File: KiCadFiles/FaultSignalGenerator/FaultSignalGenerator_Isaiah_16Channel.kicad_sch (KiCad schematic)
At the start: 18 parts, among them J1 Conn_02x20_Odd_Even, J2 Conn_02x16_Odd_Even

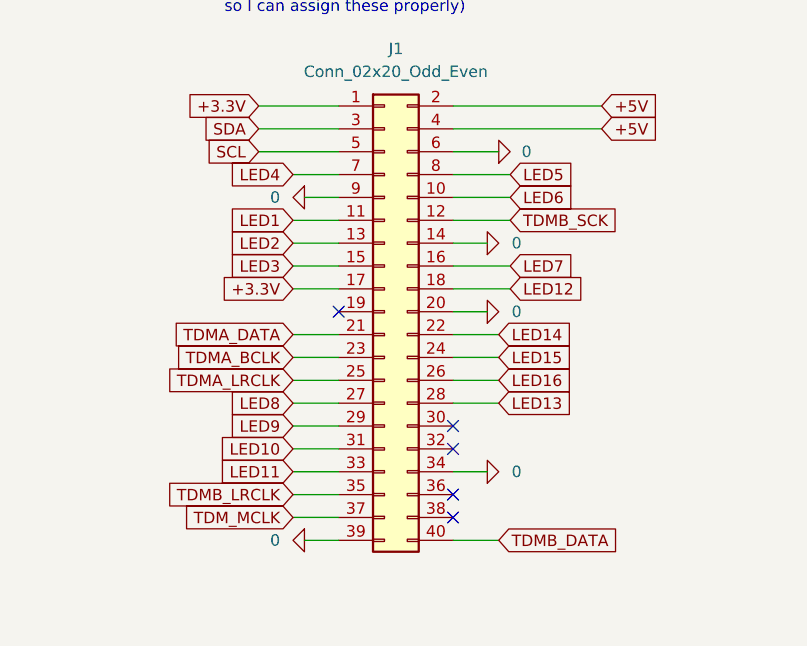
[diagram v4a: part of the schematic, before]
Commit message: Power connections + ground plane + data connections
Everything is hooked up except for the final SCL and SDA pins. I want to run them along the ground plane, but unsure if that'll cause data corruption due to EMI. Also, power connections might need to be revamped since I didn't think about series connections being a problem between components. However, this does become an issue as draw begins to increase down a single trace.
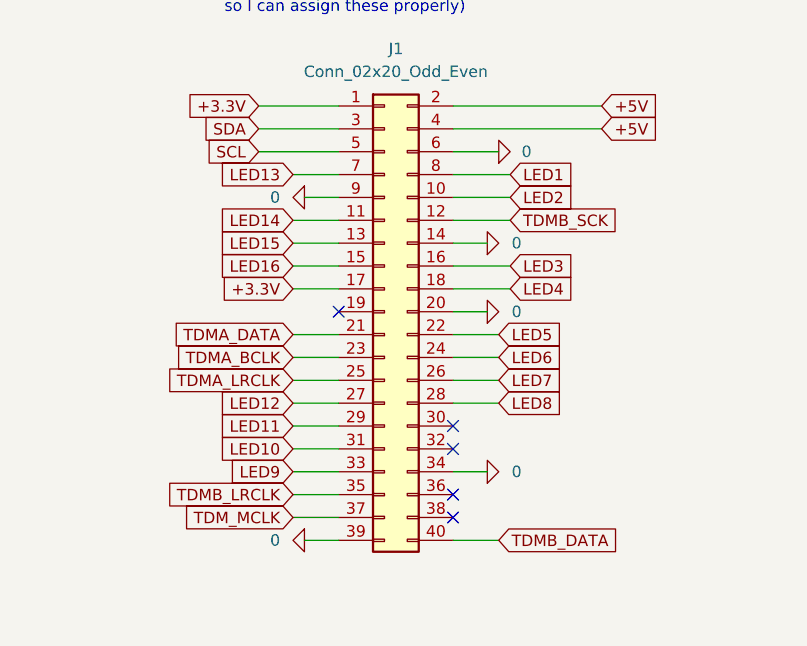
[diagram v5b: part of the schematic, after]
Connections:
- net LED1: now also J1.8 (Pin_8); no longer J1.11 (Pin_11)
- net LED11: now also J1.29 (Pin_29); no longer J1.33 (Pin_33)
- net LED12: now also J1.27 (Pin_27); no longer J1.18 (Pin_18)
- net LED13: now also J1.7 (Pin_7); no longer J1.28 (Pin_28)
- net LED14: now also J1.11 (Pin_11); no longer J1.22 (Pin_22)
- net LED15: now also J1.13 (Pin_13); no longer J1.24 (Pin_24)
- net LED16: now also J1.15 (Pin_15); no longer J1.26 (Pin_26)
- net LED2: now also J1.10 (Pin_10); no longer J1.13 (Pin_13)
- net LED3: now also J1.16 (Pin_16); no longer J1.15 (Pin_15)
- net LED4: now also J1.18 (Pin_18); no longer J1.7 (Pin_7)
- net LED5: now also J1.22 (Pin_22); no longer J1.8 (Pin_8)
- net LED6: now also J1.24 (Pin_24); no longer J1.10 (Pin_10)
- net LED7: now also J1.26 (Pin_26); no longer J1.16 (Pin_16)
- net LED8: now also J1.28 (Pin_28); no longer J1.27 (Pin_27)
- net LED9: now also J1.33 (Pin_33); no longer J1.29 (Pin_29)
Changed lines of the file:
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@@
     )
   )
-  (global_label "LED1" (shape input) (at 46.99 69.85 180) (fields_autoplaced)
-    (effects (font (size 1.27 1.27)) (justify right))
-    (property "Intersheetrefs" "${INTERSHEET_REFS}" (at 39.9202 69.7706 0)
+  (global_label "LED14" (shape input) (at 46.99 69.85 180) (fields_autoplaced)
+    (effects (font (size 1.27 1.27)) (justify right))
+    (property "Intersheetrefs" "${INTERSHEET_REFS}" (at 38.2181 69.85 0)
       (effects (font (size 1.27 1.27)) (justify right) hide)
     )
@@
     )
   )
-  (global_label "LED3" (shape input) (at 46.99 74.93 180) (fields_autoplaced)
-    (effects (font (size 1.27 1.27)) (justify right))
-    (property "Intersheetrefs" "${INTERSHEET_REFS}" (at 39.9202 74.8506 0)
-      (effects (font (size 1.27 1.27)) (justify right) hide)
-    )
-  )
-  (global_label "LED9" (shape input) (at 46.99 92.71 180) (fields_autoplaced)
-    (effects (font (size 1.27 1.27)) (justify right))
-    (property "Intersheetrefs" "${INTERSHEET_REFS}" (at 39.9202 92.6306 0)
+  (global_label "LED16" (shape input) (at 46.99 74.93 180) (fields_autoplaced)
+    (effects (font (size 1.27 1.27)) (justify right))
+    (property "Intersheetrefs" "${INTERSHEET_REFS}" (at 38.2181 74.93 0)
+      (effects (font (size 1.27 1.27)) (justify right) hide)
+    )
+  )
+  (global_label "LED11" (shape input) (at 46.99 92.71 180) (fields_autoplaced)
+    (effects (font (size 1.27 1.27)) (justify right))
+    (property "Intersheetrefs" "${INTERSHEET_REFS}" (at 38.2181 92.71 0)
       (effects (font (size 1.27 1.27)) (justify right) hide)
     )
@@
     )
   )
-  (global_label "LED6" (shape input) (at 71.12 67.31 0) (fields_autoplaced)
+  (global_label "LED2" (shape input) (at 71.12 67.31 0) (fields_autoplaced)
     (effects (font (size 1.27 1.27)) (justify left))
     (property "Intersheetrefs" "${INTERSHEET_REFS}" (at 78.6824 67.31 0)
@@
     )
   )
-  (global_label "LED14" (shape input) (at 69.85 82.55 0) (fields_autoplaced)
-    (effects (font (size 1.27 1.27)) (justify left))
-    (property "Intersheetrefs" "${INTERSHEET_REFS}" (at 78.1293 82.4706 0)
+  (global_label "LED5" (shape input) (at 69.85 82.55 0) (fields_autoplaced)
+    (effects (font (size 1.27 1.27)) (justify left))
+    (property "Intersheetrefs" "${INTERSHEET_REFS}" (at 77.4124 82.55 0)
       (effects (font (size 1.27 1.27)) (justify left) hide)
     )
@@
     )
   )
-  (global_label "LED15" (shape input) (at 69.85 85.09 0) (fields_autoplaced)
-    (effects (font (size 1.27 1.27)) (justify left))
-    (property "Intersheetrefs" "${INTERSHEET_REFS}" (at 78.1293 85.0106 0)
+  (global_label "LED6" (shape input) (at 69.85 85.09 0) (fields_autoplaced)
+    (effects (font (size 1.27 1.27)) (justify left))
+    (property "Intersheetrefs" "${INTERSHEET_REFS}" (at 77.4124 85.09 0)
       (effects (font (size 1.27 1.27)) (justify left) hide)
     )
@@
     )
   )
-  (global_label "LED2" (shape input) (at 46.99 72.39 180) (fields_autoplaced)
-    (effects (font (size 1.27 1.27)) (justify right))
-    (property "Intersheetrefs" "${INTERSHEET_REFS}" (at 39.9202 72.3106 0)
+  (global_label "LED15" (shape input) (at 46.99 72.39 180) (fields_autoplaced)
+    (effects (font (size 1.27 1.27)) (justify right))
+    (property "Intersheetrefs" "${INTERSHEET_REFS}" (at 38.2181 72.39 0)
       (effects (font (size 1.27 1.27)) (justify right) hide)
     )
@@
   (global_label "LED10" (shape input) (at 46.99 95.25 180) (fields_autoplaced)
     (effects (font (size 1.27 1.27)) (justify right))
-    (property "Intersheetrefs" "${INTERSHEET_REFS}" (at 38.7107 95.1706 0)
+    (property "Intersheetrefs" "${INTERSHEET_REFS}" (at 38.2181 95.25 0)
       (effects (font (size 1.27 1.27)) (justify right) hide)
     )
@@
     )
   )
-  (global_label "LED7" (shape input) (at 71.12 74.93 0) (fields_autoplaced)
+  (global_label "LED3" (shape input) (at 71.12 74.93 0) (fields_autoplaced)
     (effects (font (size 1.27 1.27)) (justify left))
     (property "Intersheetrefs" "${INTERSHEET_REFS}" (at 78.6824 74.93 0)
@@
     )
   )
-  (global_label "LED4" (shape input) (at 46.99 64.77 180) (fields_autoplaced)
-    (effects (font (size 1.27 1.27)) (justify right))
-    (property "Intersheetrefs" "${INTERSHEET_REFS}" (at 39.9202 64.6906 0)
-      (effects (font (size 1.27 1.27)) (justify right) hide)
-    )
-  )
-  (global_label "LED5" (shape input) (at 71.12 64.77 0) (fields_autoplaced)
+  (global_label "LED13" (shape input) (at 46.99 64.77 180) (fields_autoplaced)
+    (effects (font (size 1.27 1.27)) (justify right))
+    (property "Intersheetrefs" "${INTERSHEET_REFS}" (at 38.2181 64.77 0)
+      (effects (font (size 1.27 1.27)) (justify right) hide)
+    )
+  )
+  (global_label "LED1" (shape input) (at 71.12 64.77 0) (fields_autoplaced)
     (effects (font (size 1.27 1.27)) (justify left))
     (property "Intersheetrefs" "${INTERSHEET_REFS}" (at 78.6824 64.77 0)
@@
     )
   )
-  (global_label "LED16" (shape input) (at 69.85 87.63 0) (fields_autoplaced)
-    (effects (font (size 1.27 1.27)) (justify left))
-    (property "Intersheetrefs" "${INTERSHEET_REFS}" (at 78.1293 87.5506 0)
+  (global_label "LED7" (shape input) (at 69.85 87.63 0) (fields_autoplaced)
+    (effects (font (size 1.27 1.27)) (justify left))
+    (property "Intersheetrefs" "${INTERSHEET_REFS}" (at 77.4124 87.63 0)
       (effects (font (size 1.27 1.27)) (justify left) hide)
     )
@@
     )
   )
-  (global_label "LED12" (shape input) (at 71.12 77.47 0) (fields_autoplaced)
-    (effects (font (size 1.27 1.27)) (justify left))
-    (property "Intersheetrefs" "${INTERSHEET_REFS}" (at 79.3993 77.3906 0)
+  (global_label "LED4" (shape input) (at 71.12 77.47 0) (fields_autoplaced)
+    (effects (font (size 1.27 1.27)) (justify left))
+    (property "Intersheetrefs" "${INTERSHEET_REFS}" (at 78.6824 77.47 0)
       (effects (font (size 1.27 1.27)) (justify left) hide)
     )
@@
     )
   )
-  (global_label "LED11" (shape input) (at 46.99 97.79 180) (fields_autoplaced)
-    (effects (font (size 1.27 1.27)) (justify right))
-    (property "Intersheetrefs" "${INTERSHEET_REFS}" (at 38.7107 97.7106 0)
+  (global_label "LED9" (shape input) (at 46.99 97.79 180) (fields_autoplaced)
+    (effects (font (size 1.27 1.27)) (justify right))
+    (property "Intersheetrefs" "${INTERSHEET_REFS}" (at 39.4276 97.79 0)
       (effects (font (size 1.27 1.27)) (justify right) hide)
     )
@@
     )
   )
-  (global_label "LED8" (shape input) (at 46.99 90.17 180) (fields_autoplaced)
-    (effects (font (size 1.27 1.27)) (justify right))
-    (property "Intersheetrefs" "${INTERSHEET_REFS}" (at 39.9202 90.0906 0)
+  (global_label "LED12" (shape input) (at 46.99 90.17 180) (fields_autoplaced)
+    (effects (font (size 1.27 1.27)) (justify right))
+    (property "Intersheetrefs" "${INTERSHEET_REFS}" (at 38.2181 90.17 0)
       (effects (font (size 1.27 1.27)) (justify right) hide)
     )
@@
     )
   )
-  (global_label "LED13" (shape input) (at 69.85 90.17 0) (fields_autoplaced)
-    (effects (font (size 1.27 1.27)) (justify left))
-    (property "Intersheetrefs" "${INTERSHEET_REFS}" (at 78.1293 90.0906 0)
-      (effects (font (size 1.27 1.27)) (justify left) hide)
-    )
+  (global_label "LED8" (shape input) (at 69.85 90.17 0) (fields_autoplaced)
+    (effects (font (size 1.27 1.27)) (justify left))
+    (property "Intersheetrefs" "${INTERSHEET_REFS}" (at 77.4124 90.17 0)
+      (effects (font (size 1.27 1.27)) (justify left) hide)
+    )
